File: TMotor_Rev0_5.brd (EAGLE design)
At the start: 106.7 x 79.4 mm, 83 parts, among them U1 INA125U, U10 DEV-16771, U2 INA125U, U3 INA125U, U4 INA125U, U5 SN65HVD230MDREP

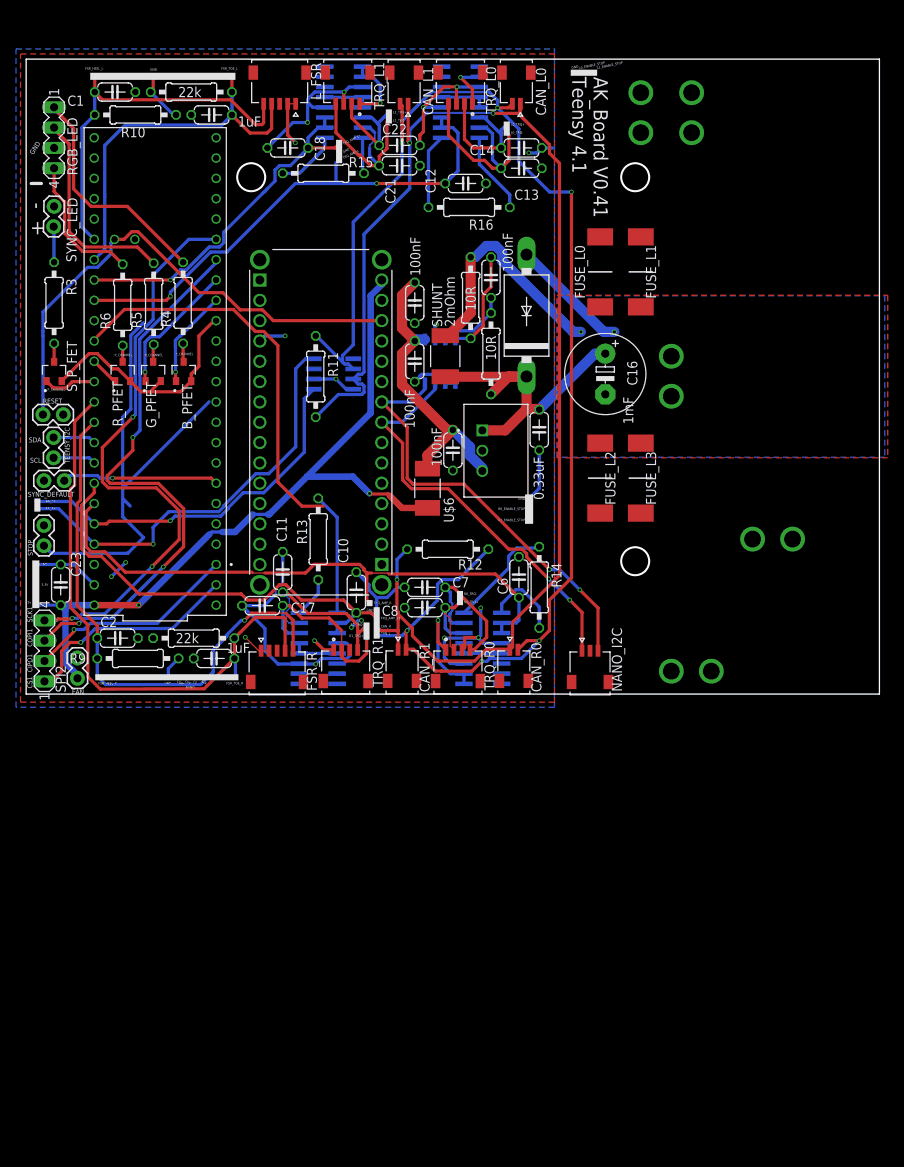
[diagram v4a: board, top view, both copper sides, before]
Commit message: Signed-off-by: NAU\cfc65 <chancecuddeback@gmail.com>
Passed DRC check. Need to perform a more rigorous manual review.
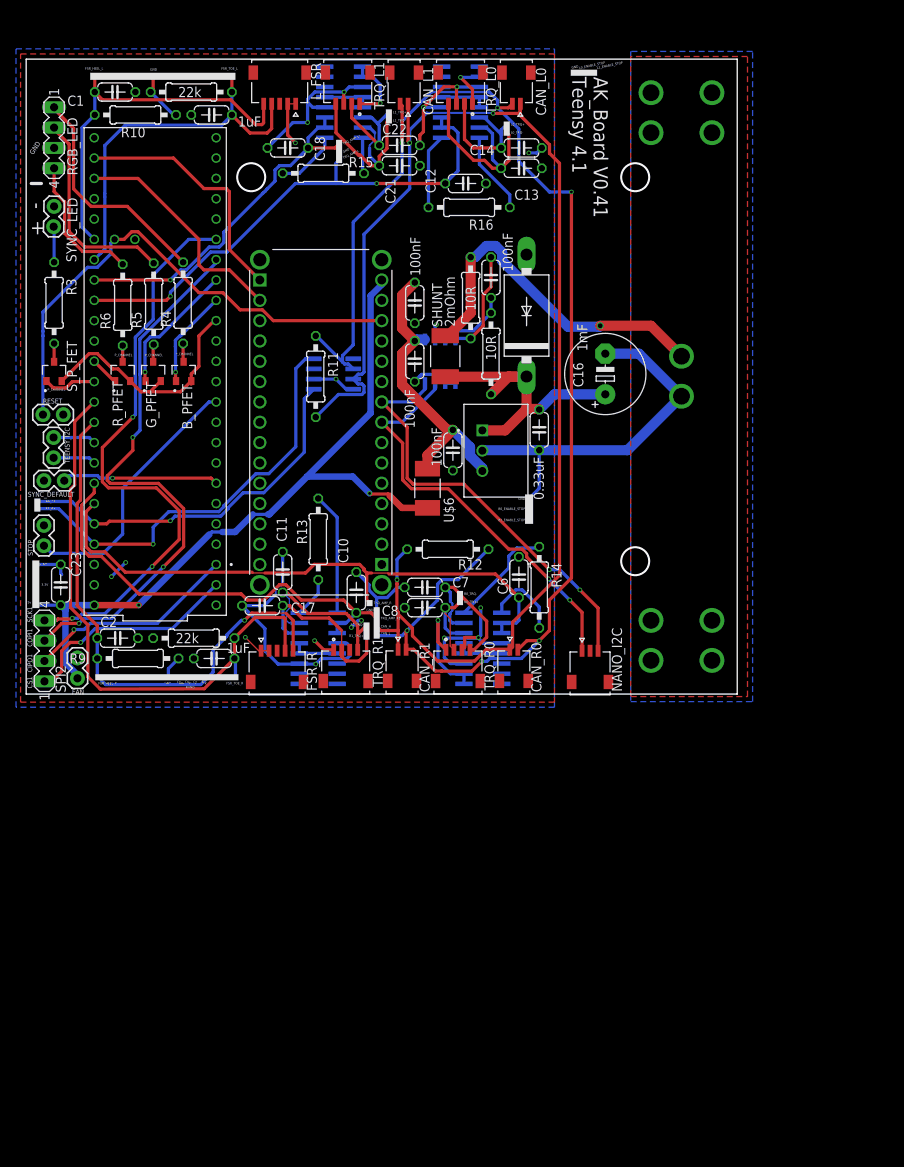
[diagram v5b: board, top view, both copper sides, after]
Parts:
- removed FUSE_L0, FUSE_L1, FUSE_L2, FUSE_L3: 0456020.ER, SamacSys_Parts:FUSC10131X312N
- moved XT30UPB-F3 11.4 mm to (52.1, 14.0), turned to 270 degrees
- moved XT30UPB-F2 6.84 mm to (44.5, 14.0), turned to 270 degrees
- moved XT30UPB-F1 2.54 mm to (52.1, 74.9)
- moved XT30UPB-F 1.27 mm to (44.5, 74.9)
- moved XT30UPB-F4 1.27 mm to (48.3, 47.0), flipped to the bottom
- turned C16 to 90 degrees
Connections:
- removed net N$43: FUSE_L1.2, XT30UPB-F1.+
- removed net N$46: FUSE_L2.2, XT30UPB-F2.+
- removed net N$47: FUSE_L3.2, XT30UPB-F3.+
- removed net N$53: FUSE_L0.2, XT30UPB-F.+
- removed net SCK: U10.13
- net STOP: now also U10.9
- net VCC1: now also XT30UPB-F.+, XT30UPB-F1.+, XT30UPB-F2.+, XT30UPB-F3.+; no longer FUSE_L0.1, FUSE_L1.1, FUSE_L2.1, FUSE_L3.1
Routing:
- net SCK: track 50.6 -> 0.00 mm
- net NANO_TX: track 0.00 -> 31.3 mm
- net NANO_RX: track 0.00 -> 28.9 mm
- net STOP: track 59.3 -> 33.1 mm
- net GND: track 164.2 -> 179.9 mm, vias 23 -> 21
- net VCC1: track 30.8 -> 44.7 mm
- net L7_VIN: track 39.0 -> 36.9 mm
- added copper zone on layer 1, net VCC1
- removed copper zone on layer 1, net VCC
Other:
- board size 106.7 x 79.4 mm -> 88.9 x 79.4 mm
- board text removed: "SCL"
- board text removed: "SDA"

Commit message: Post review
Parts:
- moved XT30UPB-F2 1.27 mm to (44.5, 12.7)
- moved XT30UPB-F3 1.27 mm to (52.1, 12.7)
- moved XT30UPB-F 1.27 mm to (44.5, 76.2)
- moved XT30UPB-F1 1.27 mm to (52.1, 76.2)
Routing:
- net GND: track 179.9 -> 178.6 mm
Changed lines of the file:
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@@
 <attribute name="VALUE" x="-33.02" y="10.795" size="1.27" layer="27" ratio="10" rot="R90"/>
 </element>
-<element name="XT30UPB-F" library="XT30UPB-F" package="XT30UPB-F" value="L_0" x="44.45" y="74.93" smashed="yes" rot="R90"/>
-<element name="XT30UPB-F1" library="XT30UPB-F" package="XT30UPB-F" value="L_0" x="52.07" y="74.93" smashed="yes" rot="R90"/>
-<element name="XT30UPB-F2" library="XT30UPB-F" package="XT30UPB-F" value="L_0" x="44.45" y="13.97" smashed="yes" rot="R270"/>
-<element name="XT30UPB-F3" library="XT30UPB-F" package="XT30UPB-F" value="L_0" x="52.07" y="13.97" smashed="yes" rot="R270"/>
+<element name="XT30UPB-F" library="XT30UPB-F" package="XT30UPB-F" value="L_0" x="44.45" y="76.2" smashed="yes" rot="R90"/>
+<element name="XT30UPB-F1" library="XT30UPB-F" package="XT30UPB-F" value="L_0" x="52.07" y="76.2" smashed="yes" rot="R90"/>
+<element name="XT30UPB-F2" library="XT30UPB-F" package="XT30UPB-F" value="L_0" x="44.45" y="12.7" smashed="yes" rot="R270"/>
+<element name="XT30UPB-F3" library="XT30UPB-F" package="XT30UPB-F" value="L_0" x="52.07" y="12.7" smashed="yes" rot="R270"/>
 <element name="XT30UPB-F4" library="XT30UPB-F" package="XT30UPB-F" value="L_0" x="48.26" y="46.99" smashed="yes" rot="MR270"/>
 </elements>
@@
 <contactref element="XT30UPB-F4" pad="-"/>
 <polygon width="0.4064" layer="16">
-<vertex x="41.91" y="85.09"/>
-<vertex x="41.91" y="3.81"/>
+<vertex x="40.64" y="84.455"/>
+<vertex x="40.64" y="3.81"/>
 <vertex x="57.15" y="3.81"/>
-<vertex x="57.15" y="85.09"/>
+<vertex x="57.15" y="84.455"/>
 </polygon>
 <wire x1="42.9425" y1="47.3075" x2="48.26" y2="41.99" width="1.27" layer="16"/>
@@
 <wire x1="15.5575" y1="44.50839375" x2="14.9225" y2="43.87339375" width="0.4064" layer="16"/>
 <wire x1="14.9225" y1="43.87339375" x2="14.9225" y2="43.815" width="0.4064" layer="16"/>
-<wire x1="-29.337" y1="20.955" x2="-29.337" y2="19.812" width="0.4064" layer="16"/>
-<wire x1="-29.337" y1="19.812" x2="-29.21" y2="19.685" width="0.4064" layer="16"/>
 </signal>
 <signal name="VIN">
@@
 <contactref element="XT30UPB-F3" pad="+"/>
 <polygon width="0.4064" layer="1">
-<vertex x="41.91" y="84.455"/>
-<vertex x="41.91" y="4.445"/>
+<vertex x="40.64" y="84.455"/>
+<vertex x="40.64" y="4.445"/>
 <vertex x="56.515" y="4.445"/>
 <vertex x="56.515" y="84.455"/>
